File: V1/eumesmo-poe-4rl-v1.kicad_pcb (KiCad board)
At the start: 4 copper layers, 99.5 x 45 mm, 125 parts, among them J1 USB_C_Receptacle_USB2.0, J2 RJ45 JACK, J3 250-202, J4 250-202, J5 250-202, J6 250-202, K1 G5NB-1A-E-DC5, K2 G5NB-1A-E-DC5, K3 G5NB-1A-E-DC5, K4 G5NB-1A-E-DC5, Q1 UMH3N, Q2 WPM2015-3/TR, Q3 LMUN2211LT1G, Q4 MMBT2222A, Q5 MMBT2222A, Q6 MMBT2222A, Q7 MMBT2222A, SW1 RESET, U1 CH340K, U2 ESP32-WROOM-32UE-N16, U3 LAN8710A, U4 TPS2376DDAR-H, U5 TX4138, U6 SY8089A1AAC

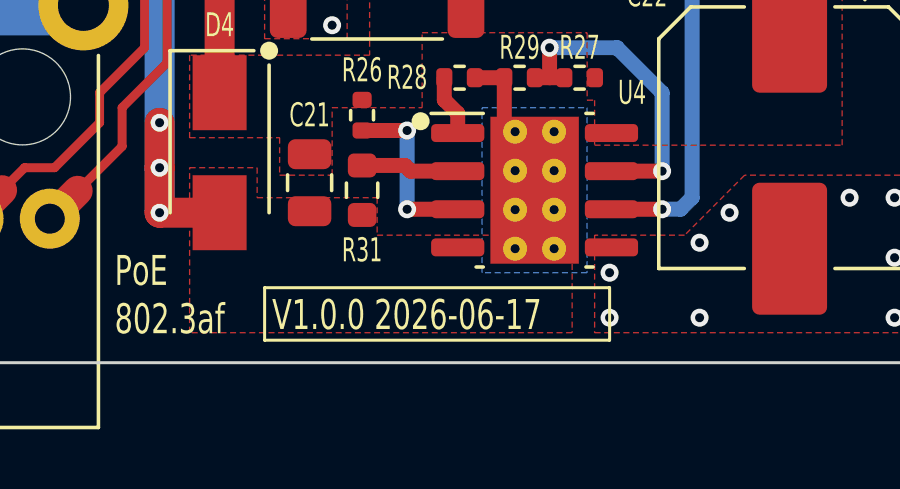
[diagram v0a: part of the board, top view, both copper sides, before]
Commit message: Added CPU health LED
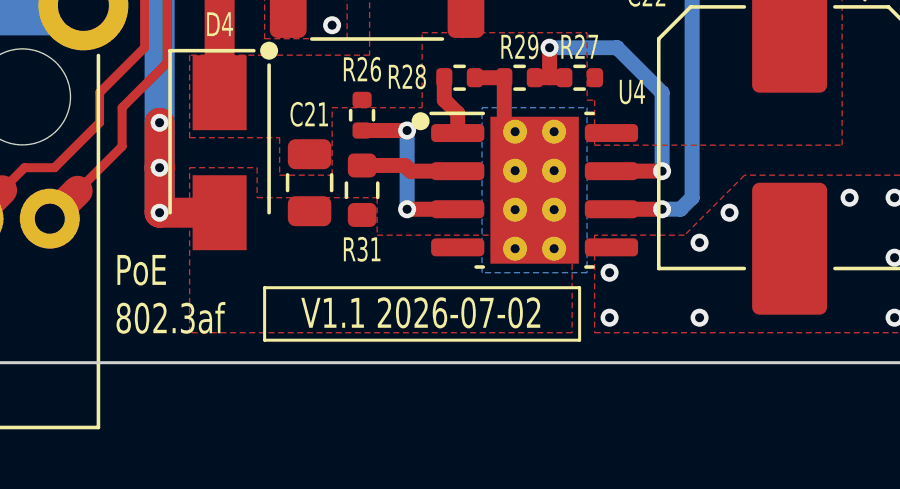
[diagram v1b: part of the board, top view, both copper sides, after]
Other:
- board text added: "V1.1 2026-07-02"
- board text removed: "V1.0.0 2026-06-17"
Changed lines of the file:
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@@
 	(gr_rect
 		(start 153 113.5)
-		(end 164.5 115.25)
+		(end 163.5 115.25)
 		(stroke
 			(width 0.1)
@@
 		)
 	)
-	(gr_text "V1.0.0 2026-06-17"
-		(at 153.25 115 0)
+	(gr_text "V1.1 2026-07-02"
+		(at 158.25 114.375 0)
 		(layer "F.SilkS")
 		(effects
@@
 				(thickness 0.1)
 			)
-			(justify left bottom)
 		)
 	)
@@
 	)
 	(segment
+		(start 132.5 93.99)
+		(end 131.5 93.99)
+		(width 0.3)
+		(layer "F.Cu")
+		(net "/CPUOK")
+	)
+	(segment
+		(start 132.5 91.6)
+		(end 131.465 91.6)
+		(width 0.5)
+		(layer "F.Cu")
+		(net "/CPUOK")
+	)
+	(via
+		(at 132.5 91.6)
+		(size 0.6)
+		(drill 0.3)
+		(layers "F.Cu" "B.Cu")
+		(net "/CPUOK")
+	)
+	(via
+		(at 132.5 93.99)
+		(size 0.6)
+		(drill 0.3)
+		(layers "F.Cu" "B.Cu")
+		(net "/CPUOK")
+	)
+	(segment
+		(start 132.5 93.99)
+		(end 132.5 91.75)
+		(width 0.3)
+		(layer "B.Cu")
+		(net "/CPUOK")
+	)
+	(segment
 		(start 129.74 94.51)
 		(end 129.4 94.85)
@@
 	)
 	(segment
+		(start 131.5 95.01)
+		(end 131.5 97.75)
+		(width 0.3)
+		(layer "F.Cu")
+		(net "/CPULED")
+	)
+	(segment
+		(start 131.5 97.75)
+		(end 130.5375 98.7125)
+		(width 0.3)
+		(layer "F.Cu")
+		(net "/CPULED")
+	)
+	(segment
+		(start 130.5375 98.7125)
+		(end 127.5 98.7125)
+		(width 0.3)
+		(layer "F.Cu")
+		(net "/CPULED")
+	)
+	(segment
 		(start 109.25 101)
 		(end 109.25 96.1)
@@
 	)
 	(segment
+		(start 138.26 76.2025)
+		(end 138.25 76.2125)
+		(width 0.5)
+		(layer "F.Cu")
+		(net "/POWER/3V3LED")
+	)
+	(segment
+		(start 138.26 73.5)
+		(end 138.26 76.2025)
+		(width 0.5)
+		(layer "F.Cu")
+		(net "/POWER/3V3LED")
+	)
+	(segment
 		(start 155.885 92.525)
 		(end 155.885 91)
@@
 		(net "/RELAY OUTPUTS/OUT2BJT")
 	)
-	(segment
-		(start 138.26 76.2025)
-		(end 138.25 76.2125)
-		(width 0.5)
-		(layer "F.Cu")
-		(net "/POWER/3V3LED")
-	)
-	(segment
-		(start 138.26 73.5)
-		(end 138.26 76.2025)
-		(width 0.5)
-		(layer "F.Cu")
-		(net "/POWER/3V3LED")
-	)
-	(segment
-		(start 131.5 95.01)
-		(end 131.5 97.75)
-		(width 0.3)
-		(layer "F.Cu")
-		(net "/CPULED")
-	)
-	(segment
-		(start 131.5 97.75)
-		(end 130.5375 98.7125)
-		(width 0.3)
-		(layer "F.Cu")
-		(net "/CPULED")
-	)
-	(segment
-		(start 130.5375 98.7125)
-		(end 127.5 98.7125)
-		(width 0.3)
-		(layer "F.Cu")
-		(net "/CPULED")
-	)
-	(segment
-		(start 132.5 93.99)
-		(end 131.5 93.99)
-		(width 0.3)
-		(layer "F.Cu")
-		(net "/CPUOK")
-	)
-	(segment
-		(start 132.5 91.6)
-		(end 131.465 91.6)
-		(width 0.5)
-		(layer "F.Cu")
-		(net "/CPUOK")
-	)
-	(via
-		(at 132.5 91.6)
-		(size 0.6)
-		(drill 0.3)
-		(layers "F.Cu" "B.Cu")
-		(net "/CPUOK")
-	)
-	(via
-		(at 132.5 93.99)
-		(size 0.6)
-		(drill 0.3)
-		(layers "F.Cu" "B.Cu")
-		(net "/CPUOK")
-	)
-	(segment
-		(start 132.5 93.99)
-		(end 132.5 91.75)
-		(width 0.3)
-		(layer "B.Cu")
-		(net "/CPUOK")
-	)
 	(zone
